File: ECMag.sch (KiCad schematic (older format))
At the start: 48 parts, among them J1 Conn_01x12, J2 Conn_01x05, J3 Conn_01x04, J4 USB_B, J5 Barrel_Jack_SW, J6 Conn_01x04, K1 Tactil Switch B3F NA, K2 Tactil Switch B3F NA, K3 Tactil Switch B3F NA, K4 Tactil Switch B3F NA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

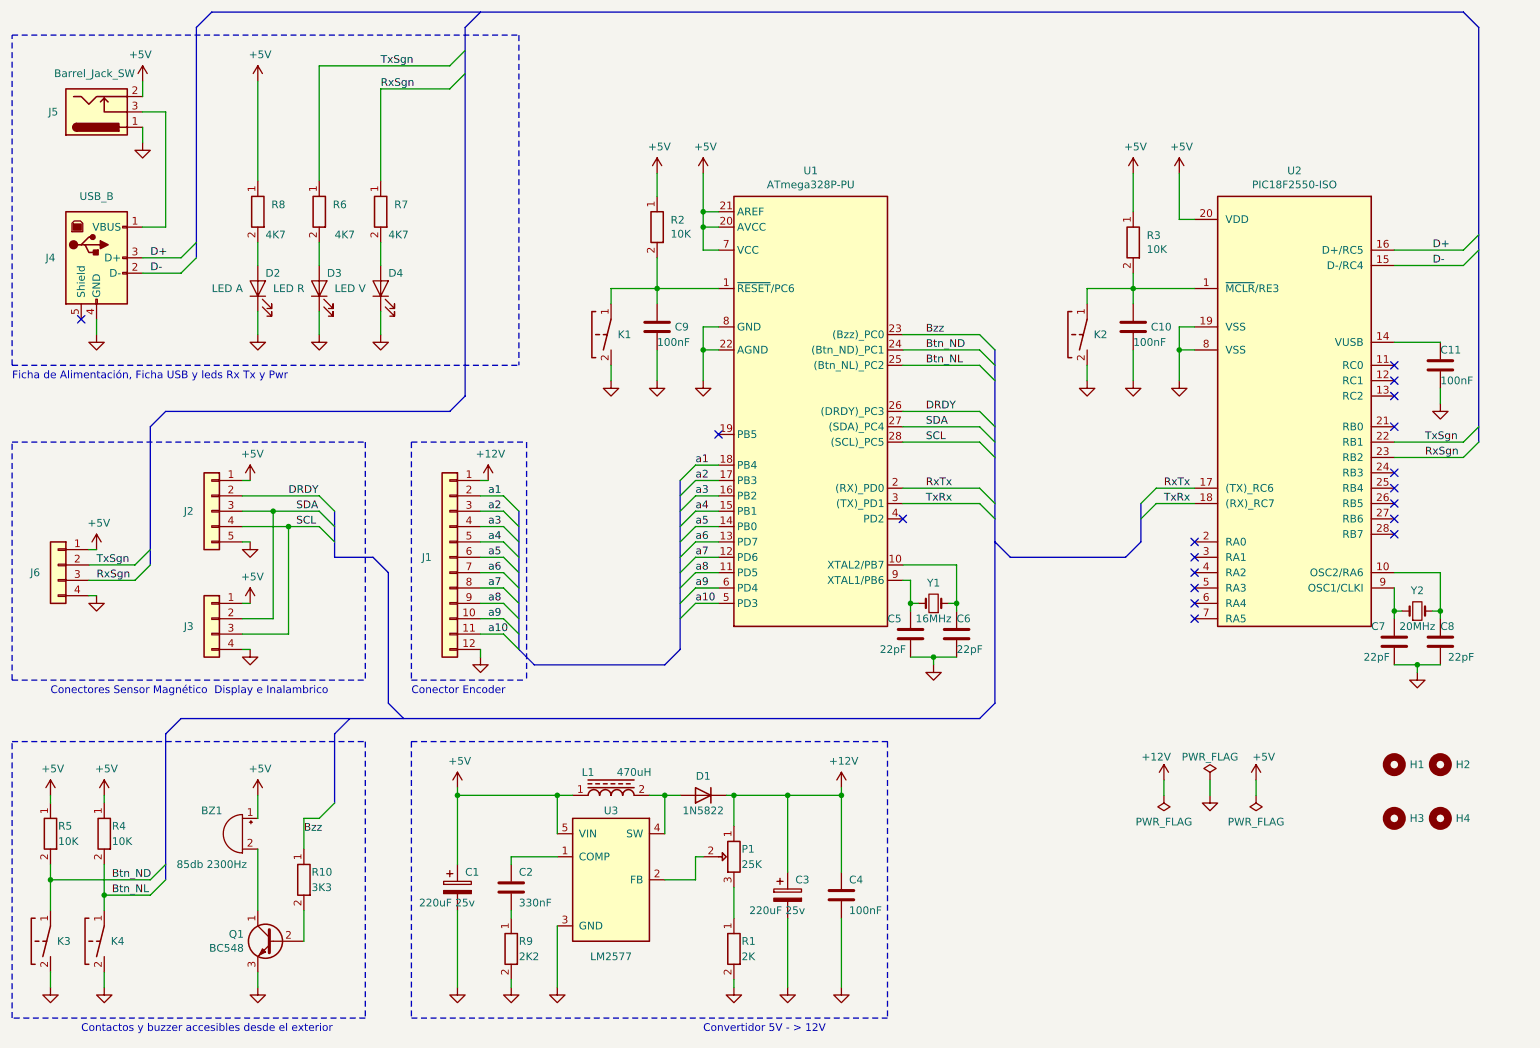
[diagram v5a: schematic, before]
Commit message: Correcciones faltantes indicadas por el profesor
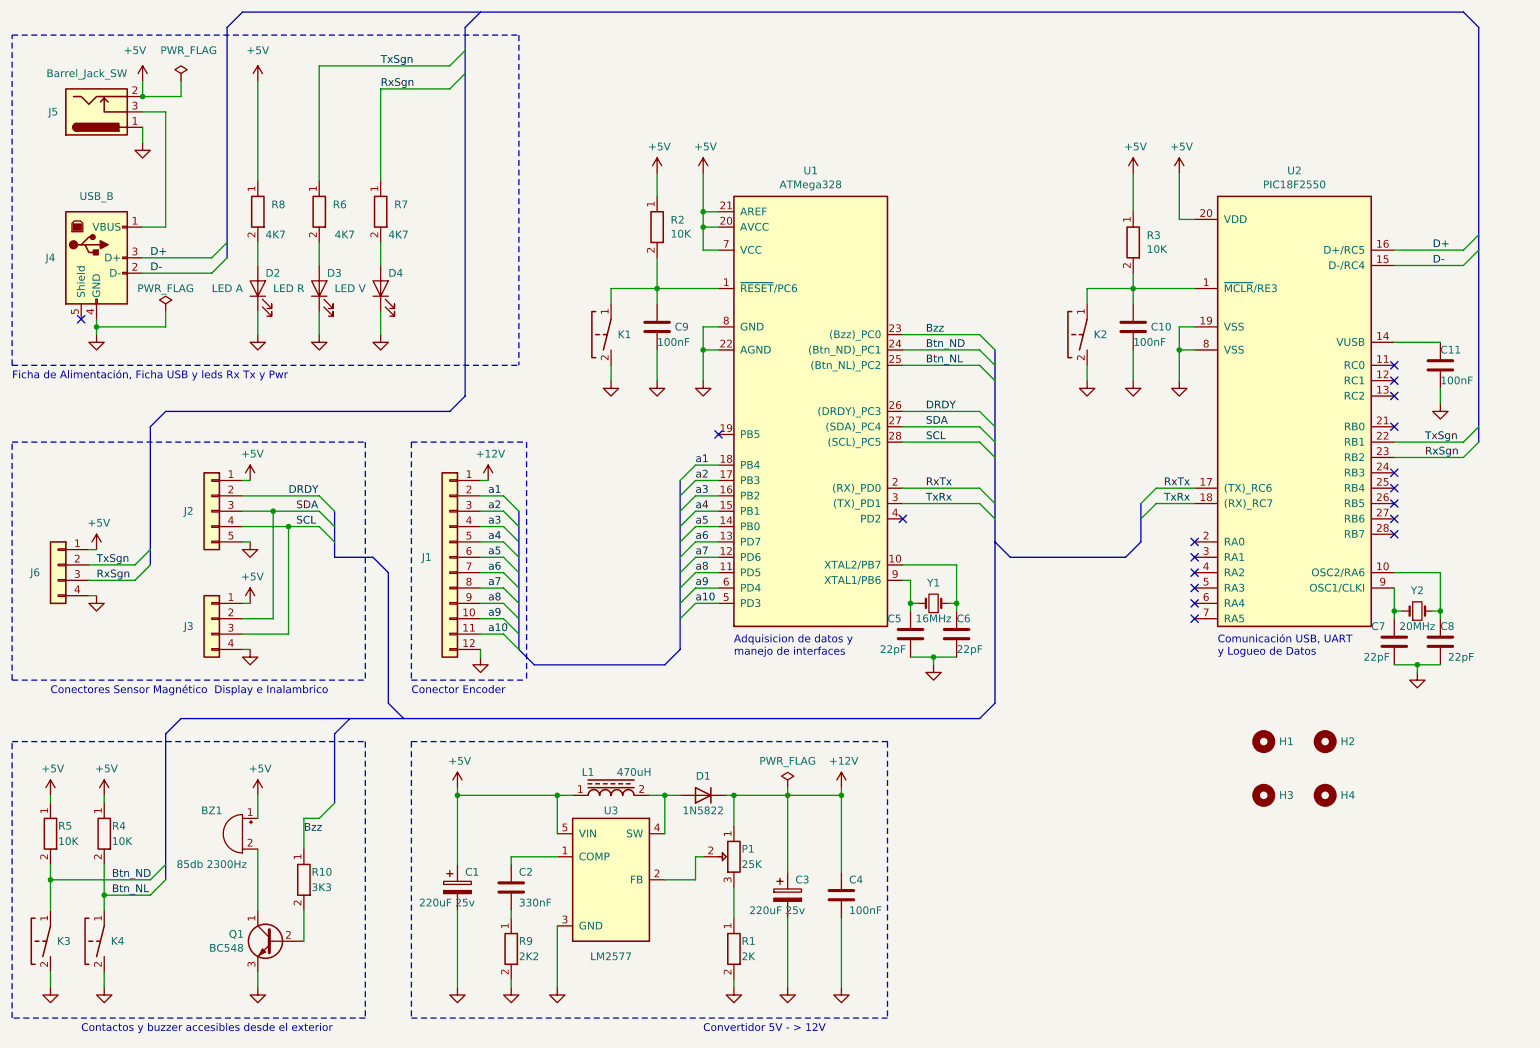
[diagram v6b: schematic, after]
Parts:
- removed U1: ATmega328P-PU, Package_DIP:DIP-28_W7.62mm, symbol Enc_Mag:ATmega328P-PU
- removed U2: PIC18F2550-ISO, Package_DIP:DIP-28_W7.62mm, symbol Enc_Mag:PIC18F2550-ISO
- added U1: ATMega328, Package_DIP:DIP-28_W7.62mm, symbol Enc_Mag:ATMega328_Enc_Mag
- added U2: PIC18F2550, Package_DIP:DIP-28_W7.62mm, symbol Enc_Mag:PIC18F2550_Enc_Mag
- BZ1: Digikey (none) -> 102-1458-ND
- D1: Digikey (none) -> 497-11370-1-ND
- J1, J2, J3, J6: Digikey (none) -> 952-3302-ND
- J4: Digikey (none) -> WM12785-ND
- J5: Digikey (none) -> CP-202A-ND
- K1, K2, K3, K4: Digikey (none) -> Z7863CT-ND
- L1: Digikey (none) -> 445-174743-2-ND
- Q1: Digikey (none) -> BC548-ND
- U3: Digikey (none) -> LM2577SX-ADJ/NOPBTR-ND
- Y1: Digikey (none) -> 1923-1788-ND
- Y2: Digikey (none) -> 1923-1441-ND
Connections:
- net +5V: now also U1.20 (AVCC), U1.21 (AREF), U1.7 (VCC), U2.20 (VDD)
- net Btn_ND: now also U1.24 ((Btn_ND)_PC1)
- net Btn_NL: now also U1.25 ((Btn_NL)_PC2)
- net Bzz: now also U1.23 ((Bzz)_PC0)
- net D+: now also U2.16 (D+/RC5)
- net D-: now also U2.15 (D-/RC4)
- net DRDY: now also U1.26 ((DRDY)_PC3)
- net GND: now also U1.22 (AGND), U1.8 (GND), U2.19 (VSS), U2.8 (VSS)
- net RxSgn: now also U2.23 (RB2)
- net RxTx: now also U1.2 ((RX)_PD0), U2.17 ((TX)_RC6)
- net SCL: now also U1.28 ((SCL)_PC5)
- net SDA: now also U1.27 ((SDA)_PC4)
- net TxRx: now also U1.3 ((TX)_PD1), U2.18 ((RX)_RC7)
- net TxSgn: now also U2.22 (RB1)
- net a1: now also U1.18 (PB4)
- net a10: now also U1.5 (PD3)
- net a2: now also U1.17 (PB3)
- net a3: now also U1.16 (PB2)
- net a4: now also U1.15 (PB1)
- net a5: now also U1.14 (PB0)
- net a6: now also U1.13 (PD7)
- net a7: now also U1.12 (PD6)
- net a8: now also U1.11 (PD5)
- net a9: now also U1.6 (PD4)
- net at C9.1, K1.1, R2.2: now also U1.1 (~RESET~/PC6)
- net at C6.1, Y1.1: now also U1.10 (XTAL2/PB7)
- net at C5.1, Y1.2: now also U1.9 (XTAL1/PB6)
- net at C10.1, K2.1, R3.2: now also U2.1 (~MCLR~/RE3)
- net at C8.1, Y2.2: now also U2.10 (OSC2/RA6)
- net at C11.1: now also U2.14 (VUSB)
- net at C7.1, Y2.1: now also U2.9 (OSC1/CLKI)
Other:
- note added: "Adquisicion de datos y \nmanejo de interfaces"
- note added: "Comunicación USB, UART \ny Logueo de Datos"
- moved on the sheet: H1, H2, H3, H4

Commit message: Correcciones faltantes indicadas por el profesor - detalles
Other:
- note added: "Conectores Sensor Magnético, Display e Inalambrico"
- note removed: "Conectores Sensor Magnético Display e Inalambrico"
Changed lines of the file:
@@
 $EndComp
 Text Notes 1200 5200 0    50   ~ 0
-Conectores Sensor Magnético  Display e Inalambrico
+Conectores Sensor Magnético,  Display e Inalambrico
 Text Notes 950  3150 0    50   ~ 0
 Ficha de Alimentación, Ficha USB y leds Rx Tx y Pwr
@@
 	1    0    0    -1
 $EndComp
-Wire Bus Line
-	8300 3950 8300 4200
-Wire Bus Line
-	1950 5450 1950 6400
-Wire Bus Line
-	1850 3450 1850 4350
-Wire Bus Line
-	2350 850  2350 2350
-Wire Bus Line
-	2450 750  10400 750
-Wire Bus Line
-	3050 4000 3050 4300
-Wire Bus Line
-	2050 5350 7250 5350
-Wire Bus Line
-	3900 850  3900 3250
-Wire Bus Line
-	10500 850  10500 3550
-Wire Bus Line
-	7350 2950 7350 5250
-Wire Bus Line
-	5300 3800 5300 4900
-Wire Bus Line
-	4250 4000 4250 4900
 Text Notes 8800 4950 0    50   ~ 0
 Comunicación USB, UART \ny Logueo de Datos
 Text Notes 5650 4950 0    50   ~ 0
 Adquisicion de datos y \nmanejo de interfaces
+Wire Bus Line
+	8300 3950 8300 4200
+Wire Bus Line
+	1950 5450 1950 6400
+Wire Bus Line
+	1850 3450 1850 4350
+Wire Bus Line
+	2350 850  2350 2350
+Wire Bus Line
+	2450 750  10400 750
+Wire Bus Line
+	3050 4000 3050 4300
+Wire Bus Line
+	2050 5350 7250 5350
+Wire Bus Line
+	3900 850  3900 3250
+Wire Bus Line
+	10500 850  10500 3550
+Wire Bus Line
+	7350 2950 7350 5250
+Wire Bus Line
+	5300 3800 5300 4900
+Wire Bus Line
+	4250 4000 4250 4900
 $EndSCHEMATC

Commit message: primera versión del pcb
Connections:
- net a1: now also U1.14 (PB0); no longer U1.18 (PB4)
- net a2: now also U1.15 (PB1); no longer U1.17 (PB3)
- net a3: now also U1.13 (PD7); no longer U1.16 (PB2)
- net a4: now also U1.16 (PB2); no longer U1.15 (PB1)
- net a5: now also U1.12 (PD6); no longer U1.14 (PB0)
- net a6: now also U1.17 (PB3); no longer U1.13 (PD7)
- net a7: now also U1.11 (PD5); no longer U1.12 (PD6)
- net a8: now also U1.18 (PB4); no longer U1.11 (PD5)
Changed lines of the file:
@@
 Comp "Pablo J.C. Alonso Castilllo"
 Comment1 "Revisor: Mauricio Barroso Benavidez"
-Comment2 "Copyright: Pablo J.C. Alonso Castillo 2020 - Todos los derechos reservados "
+Comment2 "Esta obra está bajo una Licencia Creative Commons Atribución 4.0 Internacional."
 Comment3 "CESE 10º Cohorte"
 Comment4 "Diseño de Circuitos Impresos"
@@
 a2
 Text Label 5400 3700 0    50   ~ 0
-a1
+a8
 Text Label 5400 3800 0    50   ~ 0
-a2
+a6
 Entry Wire Line
 	4150 4100 4250 4200
@@
 a10
 Text Label 5400 3900 0    50   ~ 0
+a4
+Text Label 5400 4000 0    50   ~ 0
+a2
+Text Label 5400 4100 0    50   ~ 0
+a1
+Text Label 5400 4200 0    50   ~ 0
 a3
-Text Label 5400 4000 0    50   ~ 0
-a4
-Text Label 5400 4100 0    50   ~ 0
+Text Label 5400 4300 0    50   ~ 0
 a5
-Text Label 5400 4200 0    50   ~ 0
-a6
-Text Label 5400 4300 0    50   ~ 0
+Text Label 5400 4400 0    50   ~ 0
 a7
-Text Label 5400 4400 0    50   ~ 0
-a8
 Text Label 5400 4500 0    50   ~ 0
 a9
